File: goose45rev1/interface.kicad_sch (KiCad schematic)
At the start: 13 parts, among them J1 USB_C_Receptacle_USB2.0, J2 SPI, J3 Conn_01x05_Male, J4 Debugger, J5 USART, U2 USBLC6-2SC6

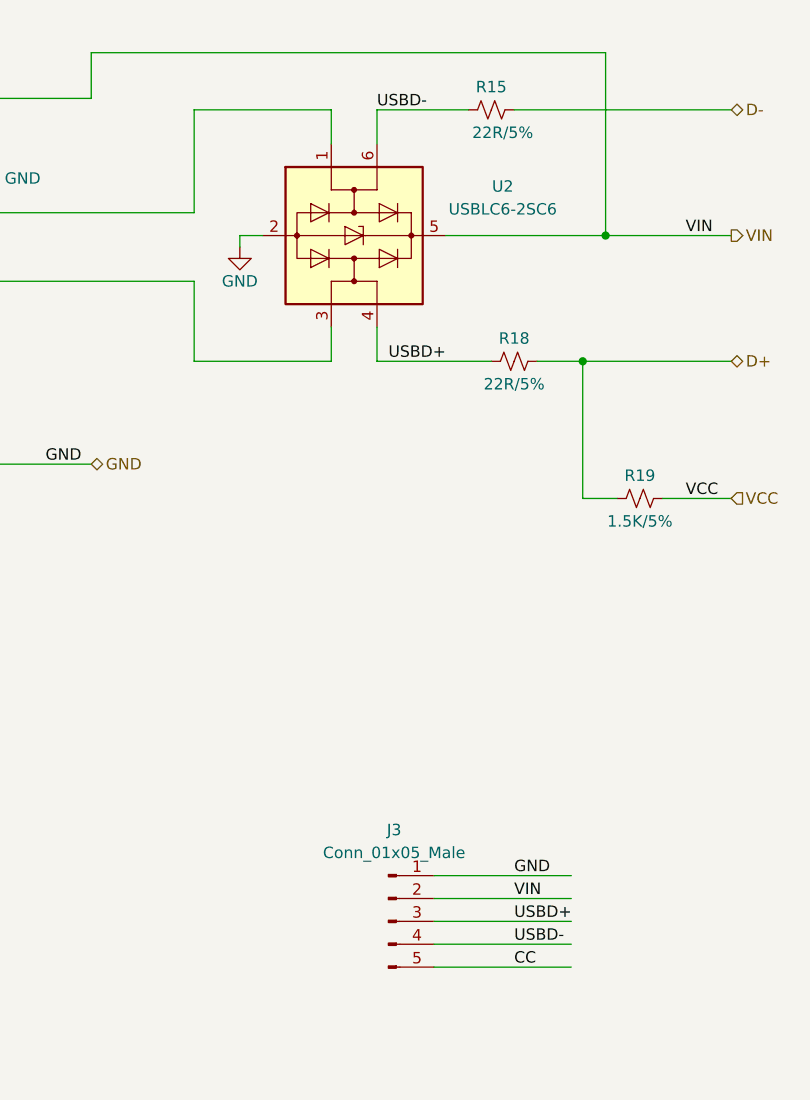
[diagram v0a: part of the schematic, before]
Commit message: move the PCB project to goose45rev1
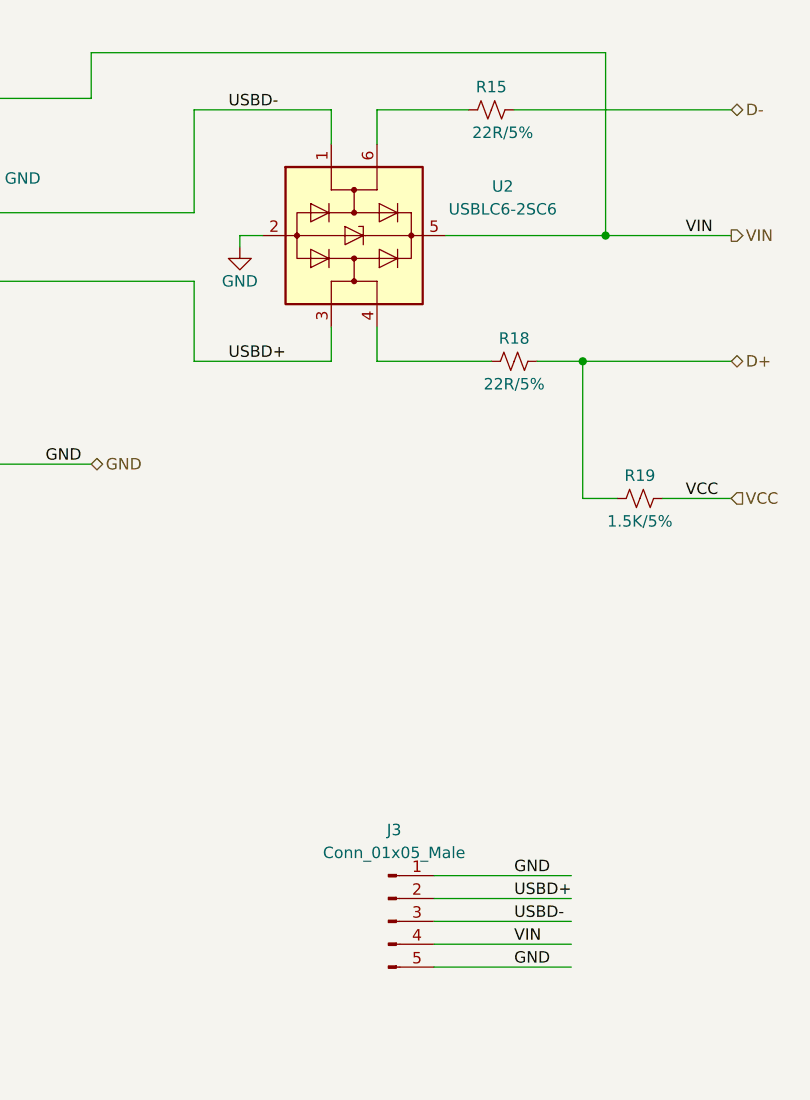
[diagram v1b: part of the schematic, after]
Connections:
- net CC: no longer J3.5 (Pin_5)
- net GND: now also J3.5 (Pin_5)
- net USBD+: now also J1.A6 (D+), J1.B6 (D+), J3.2 (Pin_2), U2.3 (I/O2); no longer J3.3 (Pin_3), R18.1, U2.4 (I/O2)
- net USBD-: now also J1.A7 (D-), J1.B7 (D-), J3.3 (Pin_3), U2.1 (I/O1); no longer J3.4 (Pin_4), R15.1, U2.6 (I/O1)
- net VIN: now also J3.4 (Pin_4); no longer J3.2 (Pin_2)
- new net: R18.1, U2.4 (I/O2)
- new net: R15.1, U2.6 (I/O1)
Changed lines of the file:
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@@
-    (effects (font (size 1.27 1.27)) (justify left bottom))
-  )
-  (label "VIN" (at 153.67 134.62 0)
     (effects (font (size 1.27 1.27)) (justify left bottom))
   )
   (label "GND" (at 242.57 88.9 0)
+    (effects (font (size 1.27 1.27)) (justify left bottom))
+  )
+  (label "USBD+" (at 121.92 74.93 0)
     (effects (font (size 1.27 1.27)) (justify left bottom))
   )
@@
     (effects (font (size 1.27 1.27)) (justify left bottom))
   )
-  (label "USBD-" (at 138.43 46.99 0)
+  (label "USBD-" (at 121.92 46.99 0)
+    (effects (font (size 1.27 1.27)) (justify left bottom))
+  )
+  (label "USBD+" (at 153.67 134.62 0)
     (effects (font (size 1.27 1.27)) (justify left bottom))
   )
@@
     (effects (font (size 1.27 1.27)) (justify left bottom))
   )
-  (label "USBD-" (at 153.67 139.7 0)
-    (effects (font (size 1.27 1.27)) (justify left bottom))
-  )
   (label "GND" (at 59.69 148.59 0)
     (effects (font (size 1.27 1.27)) (justify left bottom))
   )
-  (label "CC" (at 153.67 142.24 0)
+  (label "GND" (at 153.67 142.24 0)
+    (effects (font (size 1.27 1.27)) (justify left bottom))
+  )
+  (label "VIN" (at 153.67 139.7 0)
     (effects (font (size 1.27 1.27)) (justify left bottom))
   )
   (label "CC" (at 73.66 50.8 0)
-    (effects (font (size 1.27 1.27)) (justify left bottom))
-  )
-  (label "USBD+" (at 153.67 137.16 0)
-    (effects (font (size 1.27 1.27)) (justify left bottom))
-  )
-  (label "USBD+" (at 139.7 74.93 0)
     (effects (font (size 1.27 1.27)) (justify left bottom))
   )
@@
     (effects (font (size 1.27 1.27)) (justify left bottom))
   )
+  (label "USBD-" (at 153.67 137.16 0)
+    (effects (font (size 1.27 1.27)) (justify left bottom))
+  )

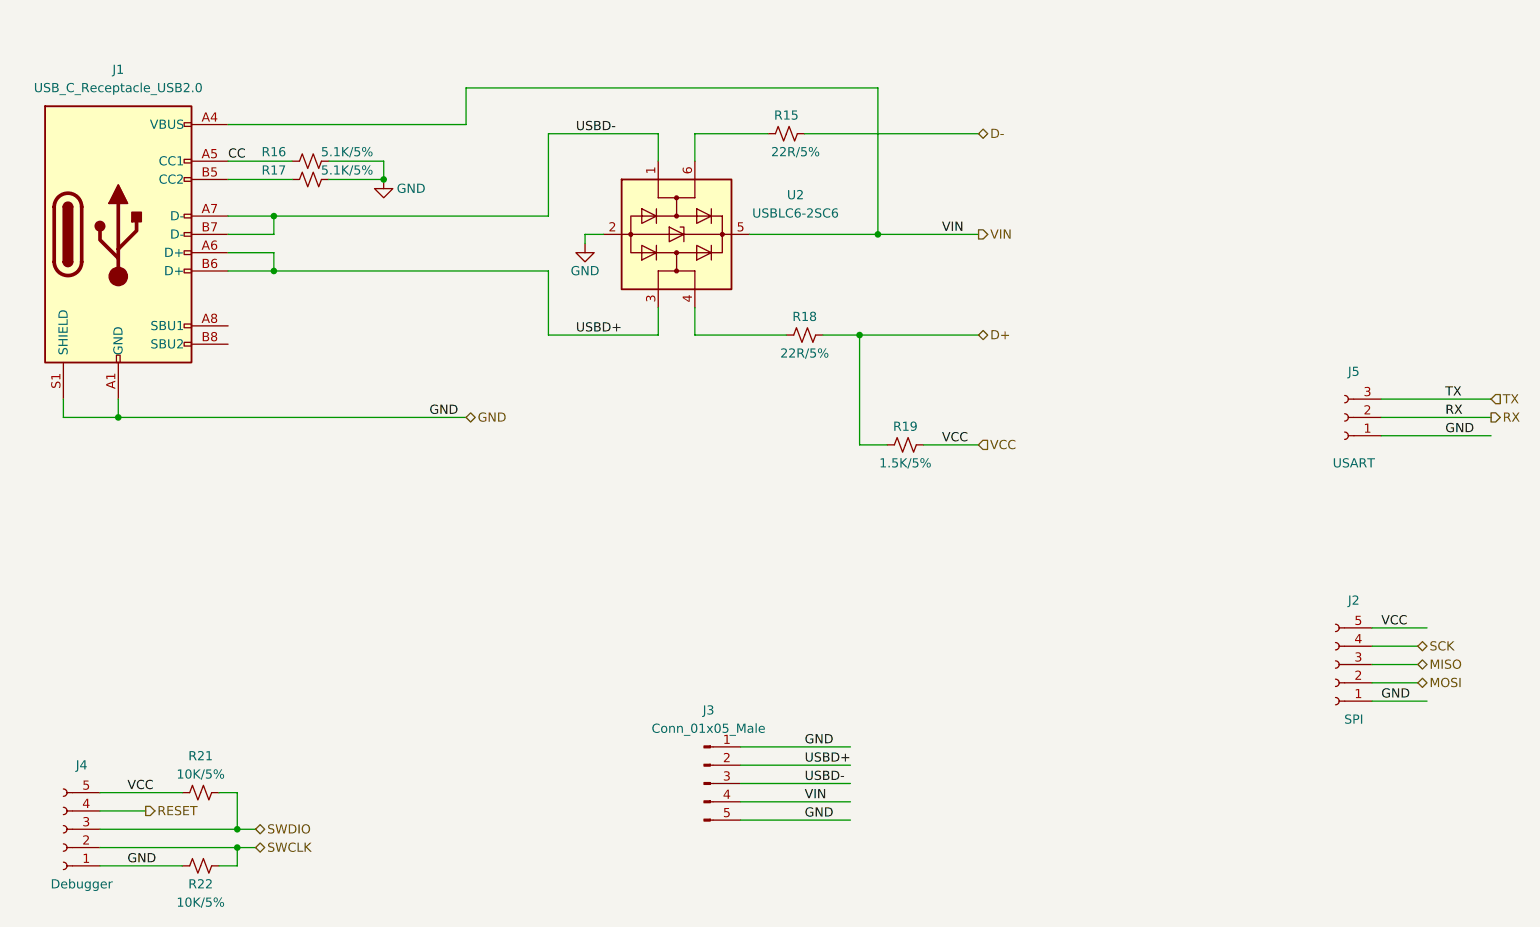
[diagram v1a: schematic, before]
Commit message: remove the usb conn on rev1
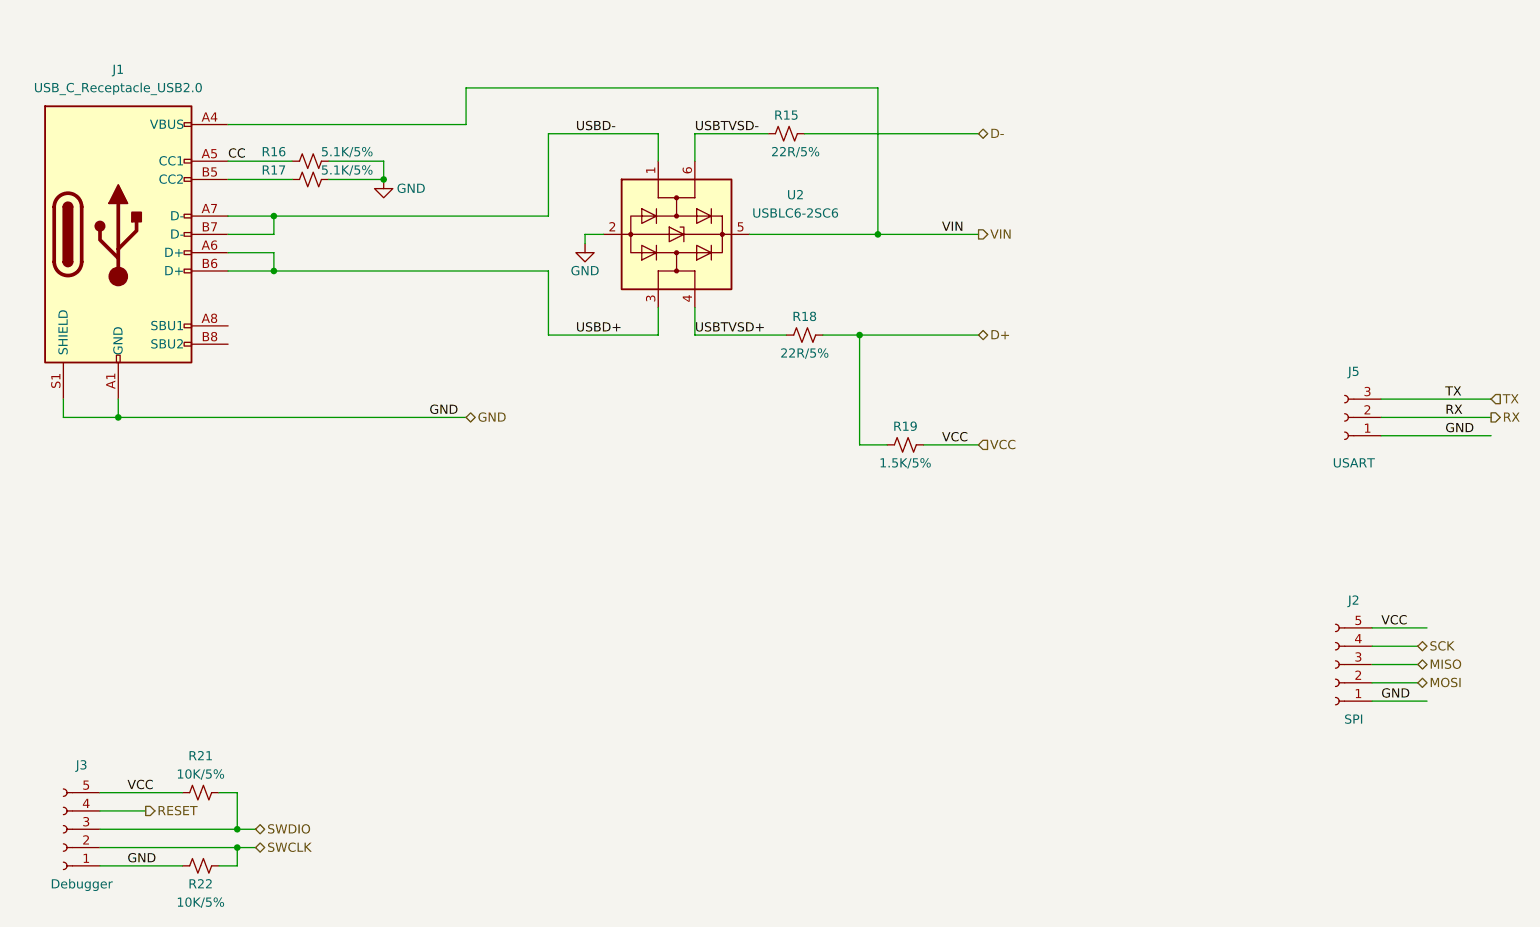
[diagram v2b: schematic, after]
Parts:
- removed J3: Conn_01x05_Male, Connector_Molex:Molex_CLIK-Mate_502386-0570_1x05-1MP_P1.25mm_Horizontal, symbol Connector:Conn_01x05_Male
- renumbered J4 to J3
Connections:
- net USBTVSD+: now reaches R18.1, U2.4 (I/O2)
- net USBTVSD-: now reaches R15.1, U2.6 (I/O1)
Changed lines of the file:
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@@
-    (stroke (width 0) (type default) (color 0 0 0 0))
-  )
-  (wire (pts (xy 144.78 134.62) (xy 160.02 134.62))
     (stroke (width 0) (type default) (color 0 0 0 0))
   )
@@
     (stroke (width 0) (type default) (color 0 0 0 0))
   )
-  (wire (pts (xy 144.78 139.7) (xy 160.02 139.7))
-    (stroke (width 0) (type default) (color 0 0 0 0))
-  )
   (wire (pts (xy 232.41 123.19) (xy 238.76 123.19))
     (stroke (width 0) (type default) (color 0 0 0 0))
@@
     (stroke (width 0) (type default) (color 0 0 0 0))
   )
-  (wire (pts (xy 144.78 137.16) (xy 160.02 137.16))
-    (stroke (width 0) (type default) (color 0 0 0 0))
-  )
   (wire (pts (xy 73.66 66.04) (xy 80.01 66.04))
     (stroke (width 0) (type default) (color 0 0 0 0))
@@
     (stroke (width 0) (type default) (color 0 0 0 0))
   )
-  (wire (pts (xy 144.78 142.24) (xy 160.02 142.24))
-    (stroke (width 0) (type default) (color 0 0 0 0))
-  )
   (wire (pts (xy 80.01 66.04) (xy 118.11 66.04))
     (stroke (width 0) (type default) (color 0 0 0 0))
@@
     (stroke (width 0) (type default) (color 0 0 0 0))
   )
-  (wire (pts (xy 144.78 132.08) (xy 160.02 132.08))
-    (stroke (width 0) (type default) (color 0 0 0 0))
-  )
   (wire (pts (xy 80.01 58.42) (xy 118.11 58.42))
     (stroke (width 0) (type default) (color 0 0 0 0))
@@
     (effects (font (size 1.27 1.27)) (justify left bottom))
   )
-  (label "GND" (at 153.67 132.08 0)
-    (effects (font (size 1.27 1.27)) (justify left bottom))
-  )
   (label "USBD-" (at 121.92 46.99 0)
     (effects (font (size 1.27 1.27)) (justify left bottom))
   )
-  (label "USBD+" (at 153.67 134.62 0)
-    (effects (font (size 1.27 1.27)) (justify left bottom))
-  )
   (label "VCC" (at 172.72 90.17 0)
     (effects (font (size 1.27 1.27)) (justify left bottom))
@@
     (effects (font (size 1.27 1.27)) (justify left bottom))
   )
-  (label "GND" (at 153.67 142.24 0)
-    (effects (font (size 1.27 1.27)) (justify left bottom))
-  )
-  (label "VIN" (at 153.67 139.7 0)
+  (label "USBTVSD+" (at 138.43 74.93 0)
+    (effects (font (size 1.27 1.27)) (justify left bottom))
+  )
+  (label "USBTVSD-" (at 138.43 46.99 0)
     (effects (font (size 1.27 1.27)) (justify left bottom))
   )
@@
   )
   (label "GND" (at 101.6 86.36 0)
-    (effects (font (size 1.27 1.27)) (justify left bottom))
-  )
-  (label "USBD-" (at 153.67 137.16 0)
     (effects (font (size 1.27 1.27)) (justify left bottom))
   )
@@
     (pin "2")
   )
-  (symbol (lib_id "Connector:Conn_01x05_Male") (at 139.7 137.16 0) (unit 1)
-    (in_bom yes) (on_board yes) (fields_autoplaced)
-    (property "Reference" "J3" (id 0) (at 140.335 127 0))
-    (property "Value" "Conn_01x05_Male" (id 1) (at 140.335 129.54 0))
-    (property "Footprint" "Connector_Molex:Molex_CLIK-Mate_502386-0570_1x05-1MP_P1.25mm_Horizontal" (id 2) (at 139.7 137.16 0)
-      (effects (font (size 1.27 1.27)) hide)
-    )
-    (property "Datasheet" "~" (id 3) (at 139.7 137.16 0)
-      (effects (font (size 1.27 1.27)) hide)
-    )
-    (pin "1")
-    (pin "2")
-    (pin "3")
-    (pin "4")
-    (pin "5")
-  )
   (symbol (lib_id "Device:R_Small_US") (at 153.67 74.93 90) (unit 1)
     (in_bom yes) (on_board yes)
@@
   (symbol (lib_id "Connector:Conn_01x05_Female") (at 50.8 143.51 180) (unit 1)
     (in_bom yes) (on_board yes)
-    (property "Reference" "J4" (id 0) (at 53.34 134.62 0))
+    (property "Reference" "J3" (id 0) (at 53.34 134.62 0))
     (property "Value" "Debugger" (id 1) (at 53.34 151.13 0))
     (property "Footprint" "Connector_PinHeader_2.00mm:PinHeader_1x05_P2.00mm_Vertical" (id 2) (at 50.8 143.51 0)

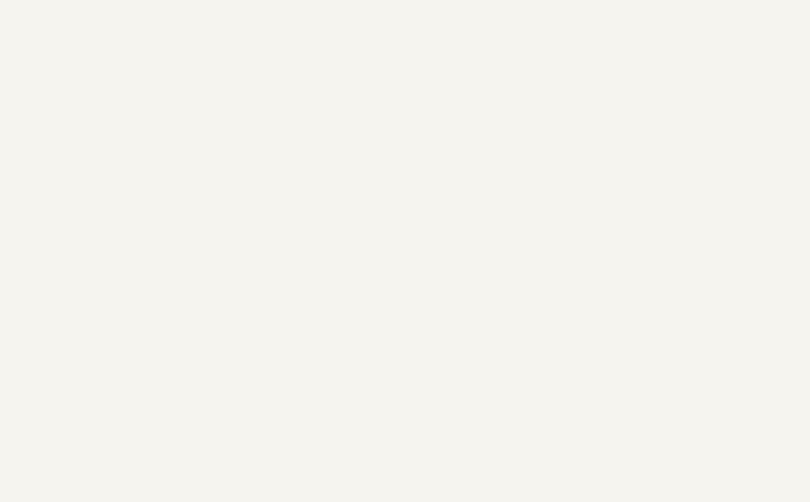
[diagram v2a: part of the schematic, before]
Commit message: update usb layout and add connector
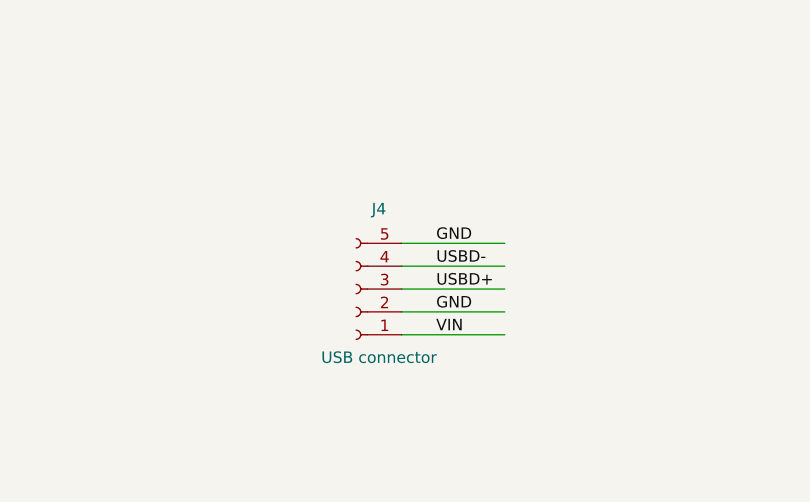
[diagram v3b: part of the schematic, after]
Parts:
- added J4: USB connector, Connector_Molex:Molex_CLIK-Mate_502386-0570_1x05-1MP_P1.25mm_Horizontal, symbol Connector:Conn_01x05_Female
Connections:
- net GND: now also J4.2 (Pin_2), J4.5 (Pin_5)
- net USBD+: now also J4.3 (Pin_3)
- net USBD-: now also J4.4 (Pin_4)
- net VIN: now also J4.1 (Pin_1)
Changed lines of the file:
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@@
+    (stroke (width 0) (type default) (color 0 0 0 0))
+  )
+  (wire (pts (xy 149.86 133.35) (xy 161.29 133.35))
     (stroke (width 0) (type default) (color 0 0 0 0))
   )
@@
     (stroke (width 0) (type default) (color 0 0 0 0))
   )
+  (wire (pts (xy 149.86 130.81) (xy 161.29 130.81))
+    (stroke (width 0) (type default) (color 0 0 0 0))
+  )
   (wire (pts (xy 232.41 123.19) (xy 238.76 123.19))
     (stroke (width 0) (type default) (color 0 0 0 0))
@@
     (stroke (width 0) (type default) (color 0 0 0 0))
   )
+  (wire (pts (xy 149.86 128.27) (xy 161.29 128.27))
+    (stroke (width 0) (type default) (color 0 0 0 0))
+  )
   (wire (pts (xy 72.39 148.59) (xy 74.93 148.59))
     (stroke (width 0) (type default) (color 0 0 0 0))
@@
     (stroke (width 0) (type default) (color 0 0 0 0))
   )
+  (wire (pts (xy 149.86 135.89) (xy 161.29 135.89))
+    (stroke (width 0) (type default) (color 0 0 0 0))
+  )
+  (wire (pts (xy 149.86 138.43) (xy 161.29 138.43))
+    (stroke (width 0) (type default) (color 0 0 0 0))
+  )
   (wire (pts (xy 87.63 53.34) (xy 95.25 53.34))
     (stroke (width 0) (type default) (color 0 0 0 0))
@@
     (effects (font (size 1.27 1.27)) (justify left bottom))
   )
+  (label "GND" (at 153.67 135.89 0)
+    (effects (font (size 1.27 1.27)) (justify left bottom))
+  )
+  (label "VIN" (at 153.67 138.43 0)
+    (effects (font (size 1.27 1.27)) (justify left bottom))
+  )
   (label "VCC" (at 172.72 90.17 0)
     (effects (font (size 1.27 1.27)) (justify left bottom))
@@
     (effects (font (size 1.27 1.27)) (justify left bottom))
   )
+  (label "USBD+" (at 153.67 133.35 0)
+    (effects (font (size 1.27 1.27)) (justify left bottom))
+  )
+  (label "USBD-" (at 153.67 130.81 0)
+    (effects (font (size 1.27 1.27)) (justify left bottom))
+  )
   (label "USBTVSD-" (at 138.43 46.99 0)
     (effects (font (size 1.27 1.27)) (justify left bottom))
@@
   )
   (label "GND" (at 101.6 86.36 0)
+    (effects (font (size 1.27 1.27)) (justify left bottom))
+  )
+  (label "GND" (at 153.67 128.27 0)
     (effects (font (size 1.27 1.27)) (justify left bottom))
   )
@@
       (effects (font (size 1.27 1.27)) hide)
     )
+    (pin "1")
+    (pin "2")
+    (pin "3")
+    (pin "4")
+    (pin "5")
+  )
+  (symbol (lib_id "Connector:Conn_01x05_Female") (at 144.78 133.35 180) (unit 1)
+    (in_bom yes) (on_board yes)
+    (property "Reference" "J4" (id 0) (at 147.32 124.46 0))
+    (property "Value" "USB connector" (id 1) (at 147.32 140.97 0))
+    (property "Footprint" "Connector_Molex:Molex_CLIK-Mate_502386-0570_1x05-1MP_P1.25mm_Horizontal" (id 2) (at 142.24 120.65 0)
+      (effects (font (size 1.27 1.27)) hide)
+    )
+    (property "Datasheet" "~" (id 3) (at 144.78 133.35 0)
+      (effects (font (size 1.27 1.27)) hide)
+    )

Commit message: update goose45 pcb usb pad and crystal
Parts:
- J4: footprint Connector_Molex:Molex_CLIK-Mate_502386-0570_1x05-1MP_P1.25mm_Horizontal -> Connector_Molex:Molex_PicoBlade_53261-0571_1x05-1MP_P1.25mm_Horizontal
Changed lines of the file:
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@@
     (property "Reference" "J4" (id 0) (at 147.32 124.46 0))
     (property "Value" "USB connector" (id 1) (at 147.32 140.97 0))
-    (property "Footprint" "Connector_Molex:Molex_CLIK-Mate_502386-0570_1x05-1MP_P1.25mm_Horizontal" (id 2) (at 142.24 120.65 0)
+    (property "Footprint" "Connector_Molex:Molex_PicoBlade_53261-0571_1x05-1MP_P1.25mm_Horizontal" (id 2) (at 142.24 120.65 0)
       (effects (font (size 1.27 1.27)) hide)
     )
